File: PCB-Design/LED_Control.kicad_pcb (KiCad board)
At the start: 2 copper layers, 60 x 80 mm, 28 parts, among them J1 5V 5A Power, J2 TO WS2812B LED STRIP, J3 Sound Sensor, SW1 SW_Push_Dual

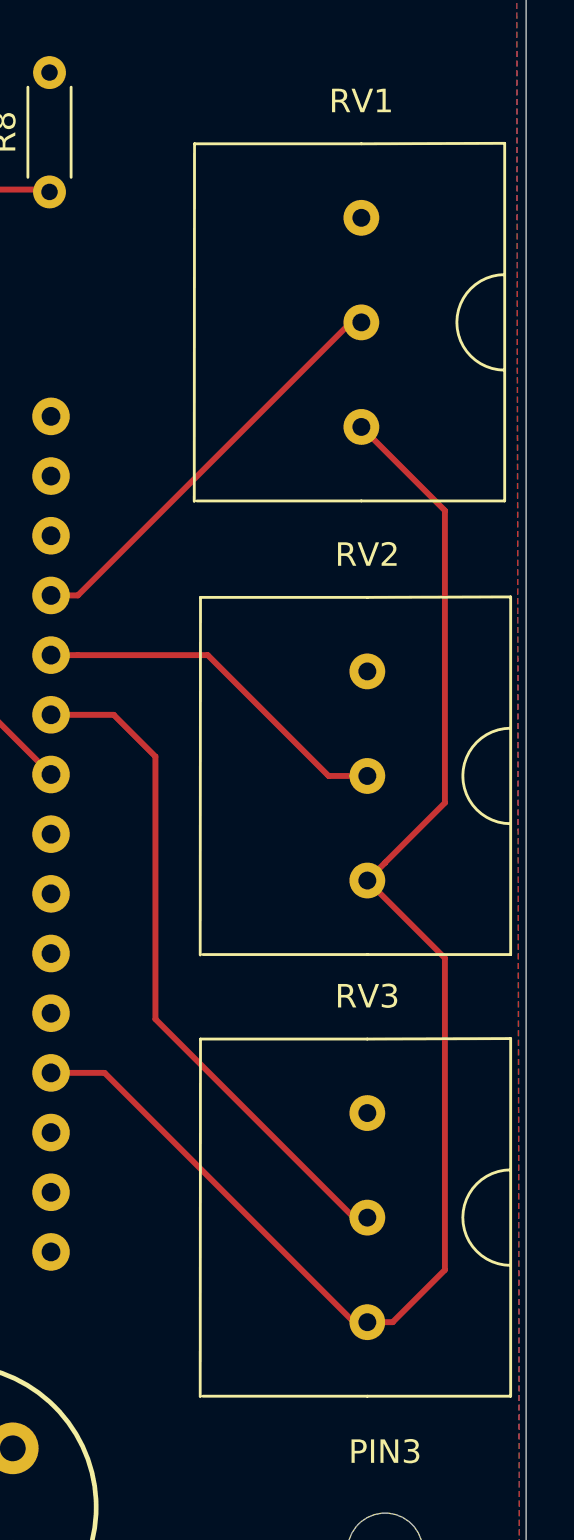
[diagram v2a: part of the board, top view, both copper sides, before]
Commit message: potentiometer footprint fixed
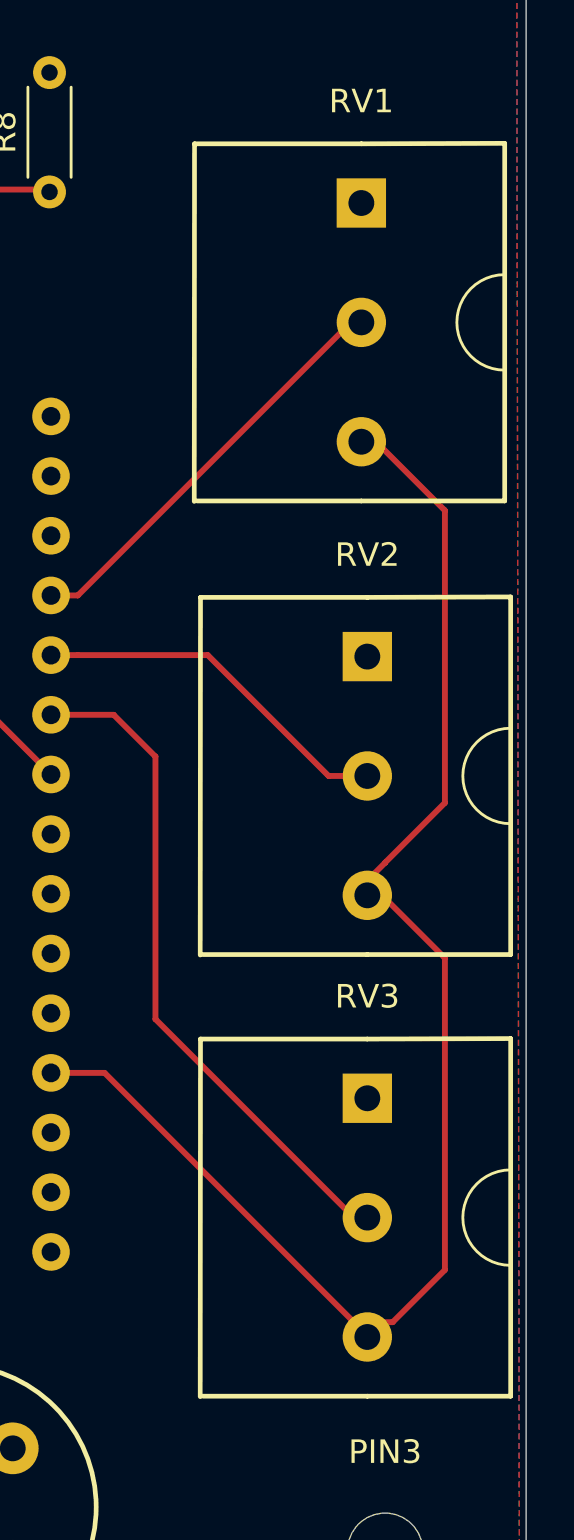
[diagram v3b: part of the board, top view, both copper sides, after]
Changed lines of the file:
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@@
     (add_net VCC)
+  )
+  (module "Custom Footprint:Potentiometer_4mm_Pitch" (layer F.Cu)
+    (at 158.242 119.8245)
+    (fp_text reference RV3 (at 0 -9.406) (layer F.SilkS)
+      (effects (font (size 1 1) (thickness 0.15)))
+    )
+    (fp_text value 100k (at -5.5245 8.8265) (layer F.Fab)
+      (effects (font (size 1 1) (thickness 0.15)))
+    )
+    (fp_line (start 6.096 7.62) (end -7.112 7.62) (layer F.Fab) (width 0.12))
+    (fp_line (start 6.096 -7.62) (end 6.096 7.62) (layer F.Fab) (width 0.12))
+    (fp_line (start -7.112 -7.62) (end 6.096 -7.62) (layer F.Fab) (width 0.12))
+    (fp_line (start -7.112 -7.62) (end -7.112 7.62) (layer F.Fab) (width 0.12))
+    (fp_arc (start 6.096 0) (end 6.096 -2.032) (angle -180) (layer F.SilkS) (width 0.12))
+    (fp_line (start 6.1 -7.62) (end 6.1 7.6) (layer F.SilkS) (width 0.2))
+    (fp_line (start 0 7.6) (end 6.1 7.6) (layer F.SilkS) (width 0.2))
+    (fp_line (start 0 -7.6) (end 6.1 -7.62) (layer F.SilkS) (width 0.2))
+    (fp_line (start -7.1 -7.6) (end -7.112 7.62) (layer F.SilkS) (width 0.2))
+    (fp_line (start 0 7.6) (end -7 7.6) (layer F.SilkS) (width 0.2))
+    (fp_line (start 0 -7.6) (end -7.1 -7.6) (layer F.SilkS) (width 0.2))
+    (pad 3 thru_hole circle (at 0 5.08) (size 2.1 2.1) (drill 1.1) (layers *.Cu *.Mask)
+      (net 21 "Net-(A1-Pad27)"))
+    (pad 2 thru_hole circle (at 0 0) (size 2.1 2.1) (drill 1.1) (layers *.Cu *.Mask)
+      (net 10 "Net-(A1-Pad21)"))
+    (pad 1 thru_hole trapezoid (at 0 -5.08) (size 2.1 2.1) (drill 1.1) (layers *.Cu *.Mask)
+      (net 25 GND))
+  )
+  (module "Custom Footprint:Potentiometer_4mm_Pitch" (layer F.Cu)
+    (at 158.242 101.0285)
+    (fp_text reference RV2 (at 0 -9.406) (layer F.SilkS)
+      (effects (font (size 1 1) (thickness 0.15)))
+    )
+    (fp_text value 100k (at -5.334 8.6995) (layer F.Fab)
+      (effects (font (size 1 1) (thickness 0.15)))
+    )
+    (fp_line (start 6.096 7.62) (end -7.112 7.62) (layer F.Fab) (width 0.12))
+    (fp_line (start 6.096 -7.62) (end 6.096 7.62) (layer F.Fab) (width 0.12))
+    (fp_line (start -7.112 -7.62) (end 6.096 -7.62) (layer F.Fab) (width 0.12))
+    (fp_line (start -7.112 -7.62) (end -7.112 7.62) (layer F.Fab) (width 0.12))
+    (fp_arc (start 6.096 0) (end 6.096 -2.032) (angle -180) (layer F.SilkS) (width 0.12))
+    (fp_line (start 6.1 -7.62) (end 6.1 7.6) (layer F.SilkS) (width 0.2))
+    (fp_line (start 0 7.6) (end 6.1 7.6) (layer F.SilkS) (width 0.2))
+    (fp_line (start 0 -7.6) (end 6.1 -7.62) (layer F.SilkS) (width 0.2))
+    (fp_line (start -7.1 -7.6) (end -7.112 7.62) (layer F.SilkS) (width 0.2))
+    (fp_line (start 0 7.6) (end -7 7.6) (layer F.SilkS) (width 0.2))
+    (fp_line (start 0 -7.6) (end -7.1 -7.6) (layer F.SilkS) (width 0.2))
+    (pad 3 thru_hole circle (at 0 5.08) (size 2.1 2.1) (drill 1.1) (layers *.Cu *.Mask)
+      (net 21 "Net-(A1-Pad27)"))
+    (pad 2 thru_hole circle (at 0 0) (size 2.1 2.1) (drill 1.1) (layers *.Cu *.Mask)
+      (net 8 "Net-(A1-Pad20)"))
+    (pad 1 thru_hole trapezoid (at 0 -5.08) (size 2.1 2.1) (drill 1.1) (layers *.Cu *.Mask)
+      (net 25 GND))
+  )
+  (module "Custom Footprint:Potentiometer_4mm_Pitch" (layer F.Cu)
+    (at 157.988 81.7245)
+    (fp_text reference RV1 (at 0 -9.406) (layer F.SilkS)
+      (effects (font (size 1 1) (thickness 0.15)))
+    )
+    (fp_text value 100k (at -4.953 8.6995) (layer F.Fab)
+      (effects (font (size 1 1) (thickness 0.15)))
+    )
+    (fp_line (start 6.096 7.62) (end -7.112 7.62) (layer F.Fab) (width 0.12))
+    (fp_line (start 6.096 -7.62) (end 6.096 7.62) (layer F.Fab) (width 0.12))
+    (fp_line (start -7.112 -7.62) (end 6.096 -7.62) (layer F.Fab) (width 0.12))
+    (fp_line (start -7.112 -7.62) (end -7.112 7.62) (layer F.Fab) (width 0.12))
+    (fp_arc (start 6.096 0) (end 6.096 -2.032) (angle -180) (layer F.SilkS) (width 0.12))
+    (fp_line (start 6.1 -7.62) (end 6.1 7.6) (layer F.SilkS) (width 0.2))
+    (fp_line (start 0 7.6) (end 6.1 7.6) (layer F.SilkS) (width 0.2))
+    (fp_line (start 0 -7.6) (end 6.1 -7.62) (layer F.SilkS) (width 0.2))
+    (fp_line (start -7.1 -7.6) (end -7.112 7.62) (layer F.SilkS) (width 0.2))
+    (fp_line (start 0 7.6) (end -7 7.6) (layer F.SilkS) (width 0.2))
+    (fp_line (start 0 -7.6) (end -7.1 -7.6) (layer F.SilkS) (width 0.2))
+    (pad 3 thru_hole circle (at 0 5.08) (size 2.1 2.1) (drill 1.1) (layers *.Cu *.Mask)
+      (net 21 "Net-(A1-Pad27)"))
+    (pad 2 thru_hole circle (at 0 0) (size 2.1 2.1) (drill 1.1) (layers *.Cu *.Mask)
+      (net 6 "Net-(A1-Pad19)"))
+    (pad 1 thru_hole trapezoid (at 0 -5.08) (size 2.1 2.1) (drill 1.1) (layers *.Cu *.Mask)
+      (net 25 GND))
   )
   (module Resistor_THT:R_Axial_DIN0204_L3.6mm_D1.6mm_P5.08mm_Horizontal (layer F.Cu)
@@
     )
   )
-  (module "Custom Footprint:Potentiometer_4mm_Pitch" (layer F.Cu)
-    (at 157.988 81.7245)
-    (fp_text reference RV1 (at 0 -9.406) (layer F.SilkS)
-      (effects (font (size 1 1) (thickness 0.15)))
-    )
-    (fp_text value 100k (at -4.953 8.6995) (layer F.Fab)
-      (effects (font (size 1 1) (thickness 0.15)))
-    )
-    (fp_arc (start 6.096 0) (end 6.096 -2.032) (angle -180) (layer F.SilkS) (width 0.12))
-    (fp_line (start 6.1 -7.62) (end 6.1 7.6) (layer F.SilkS) (width 0.12))
-    (fp_line (start 0 7.6) (end 6.1 7.6) (layer F.SilkS) (width 0.12))
-    (fp_line (start 0 -7.6) (end 6.1 -7.62) (layer F.SilkS) (width 0.12))
-    (fp_line (start -7.1 -7.6) (end -7.112 7.62) (layer F.SilkS) (width 0.12))
-    (fp_line (start 0 7.6) (end -7 7.6) (layer F.SilkS) (width 0.12))
-    (fp_line (start 0 -7.6) (end -7.1 -7.6) (layer F.SilkS) (width 0.12))
-    (pad 3 thru_hole circle (at 0 4.45) (size 1.524 1.524) (drill 0.762) (layers *.Cu *.Mask)
-      (net 21 "Net-(A1-Pad27)"))
-    (pad 2 thru_hole circle (at 0 0) (size 1.524 1.524) (drill 0.762) (layers *.Cu *.Mask)
-      (net 6 "Net-(A1-Pad19)"))
-    (pad 1 thru_hole circle (at 0 -4.45) (size 1.524 1.524) (drill 0.762) (layers *.Cu *.Mask)
-      (net 25 GND))
-  )
-  (module "Custom Footprint:Potentiometer_4mm_Pitch" (layer F.Cu)
-    (at 158.242 101.0285)
-    (fp_text reference RV2 (at 0 -9.406) (layer F.SilkS)
-      (effects (font (size 1 1) (thickness 0.15)))
-    )
-    (fp_text value 100k (at -5.334 8.6995) (layer F.Fab)
-      (effects (font (size 1 1) (thickness 0.15)))
-    )
-    (fp_line (start 0 -7.6) (end -7.1 -7.6) (layer F.SilkS) (width 0.12))
-    (fp_line (start 0 7.6) (end -7 7.6) (layer F.SilkS) (width 0.12))
-    (fp_line (start -7.1 -7.6) (end -7.112 7.62) (layer F.SilkS) (width 0.12))
-    (fp_line (start 0 -7.6) (end 6.1 -7.62) (layer F.SilkS) (width 0.12))
-    (fp_line (start 0 7.6) (end 6.1 7.6) (layer F.SilkS) (width 0.12))
-    (fp_line (start 6.1 -7.62) (end 6.1 7.6) (layer F.SilkS) (width 0.12))
-    (fp_arc (start 6.096 0) (end 6.096 -2.032) (angle -180) (layer F.SilkS) (width 0.12))
-    (pad 1 thru_hole circle (at 0 -4.45) (size 1.524 1.524) (drill 0.762) (layers *.Cu *.Mask)
-      (net 25 GND))
-    (pad 2 thru_hole circle (at 0 0) (size 1.524 1.524) (drill 0.762) (layers *.Cu *.Mask)
-      (net 8 "Net-(A1-Pad20)"))
-    (pad 3 thru_hole circle (at 0 4.45) (size 1.524 1.524) (drill 0.762) (layers *.Cu *.Mask)
-      (net 21 "Net-(A1-Pad27)"))
-  )
-  (module "Custom Footprint:Potentiometer_4mm_Pitch" (layer F.Cu)
-    (at 158.242 119.8245)
-    (fp_text reference RV3 (at 0 -9.406) (layer F.SilkS)
-      (effects (font (size 1 1) (thickness 0.15)))
-    )
-    (fp_text value 100k (at -5.5245 8.8265) (layer F.Fab)
-      (effects (font (size 1 1) (thickness 0.15)))
-    )
-    (fp_line (start 0 -7.6) (end -7.1 -7.6) (layer F.SilkS) (width 0.12))
-    (fp_line (start 0 7.6) (end -7 7.6) (layer F.SilkS) (width 0.12))
-    (fp_line (start -7.1 -7.6) (end -7.112 7.62) (layer F.SilkS) (width 0.12))
-    (fp_line (start 0 -7.6) (end 6.1 -7.62) (layer F.SilkS) (width 0.12))
-    (fp_line (start 0 7.6) (end 6.1 7.6) (layer F.SilkS) (width 0.12))
-    (fp_line (start 6.1 -7.62) (end 6.1 7.6) (layer F.SilkS) (width 0.12))
-    (fp_arc (start 6.096 0) (end 6.096 -2.032) (angle -180) (layer F.SilkS) (width 0.12))
-    (pad 1 thru_hole circle (at 0 -4.45) (size 1.524 1.524) (drill 0.762) (layers *.Cu *.Mask)
-      (net 25 GND))
-    (pad 2 thru_hole circle (at 0 0) (size 1.524 1.524) (drill 0.762) (layers *.Cu *.Mask)
-      (net 10 "Net-(A1-Pad21)"))
-    (pad 3 thru_hole circle (at 0 4.45) (size 1.524 1.524) (drill 0.762) (layers *.Cu *.Mask)
-      (net 21 "Net-(A1-Pad27)"))
-  )
   (module "Custom Footprint:Push_Button_Switch" (layer F.Cu)

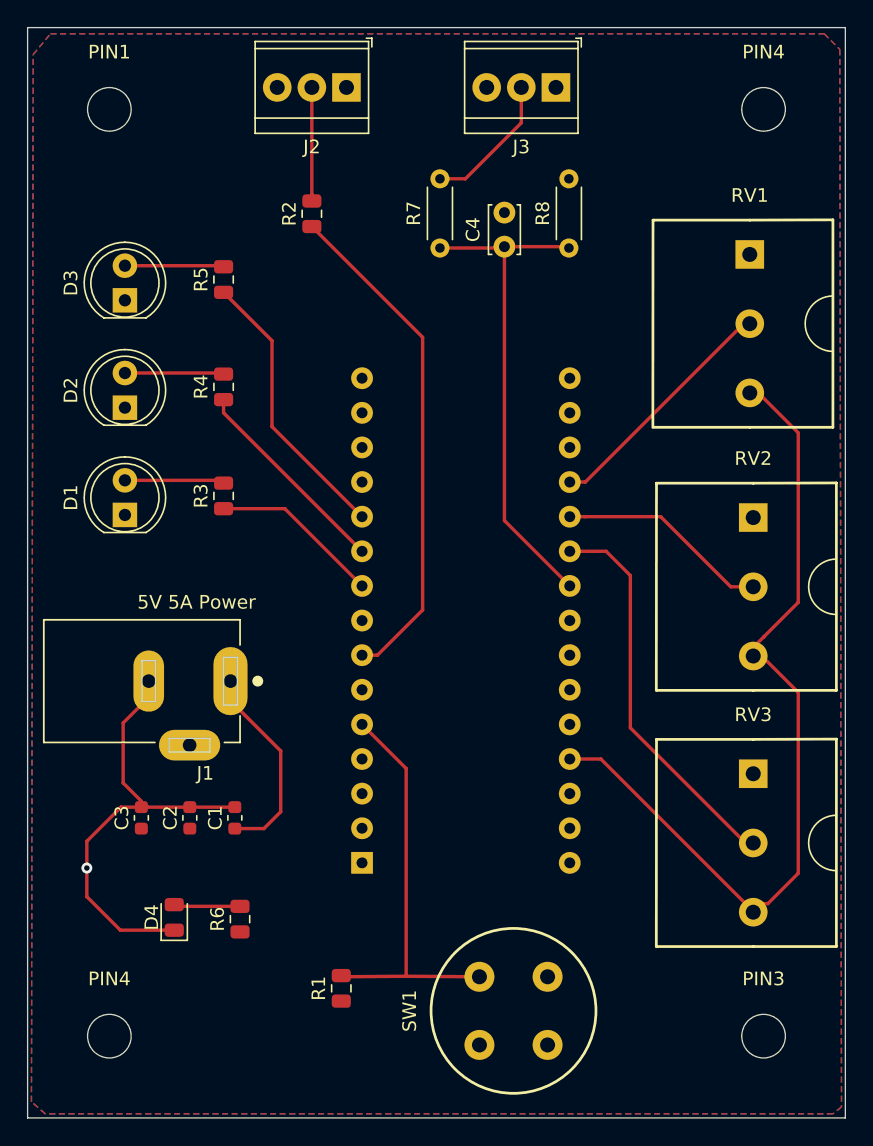
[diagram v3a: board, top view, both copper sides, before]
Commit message: Rev 2. alterations to PCB
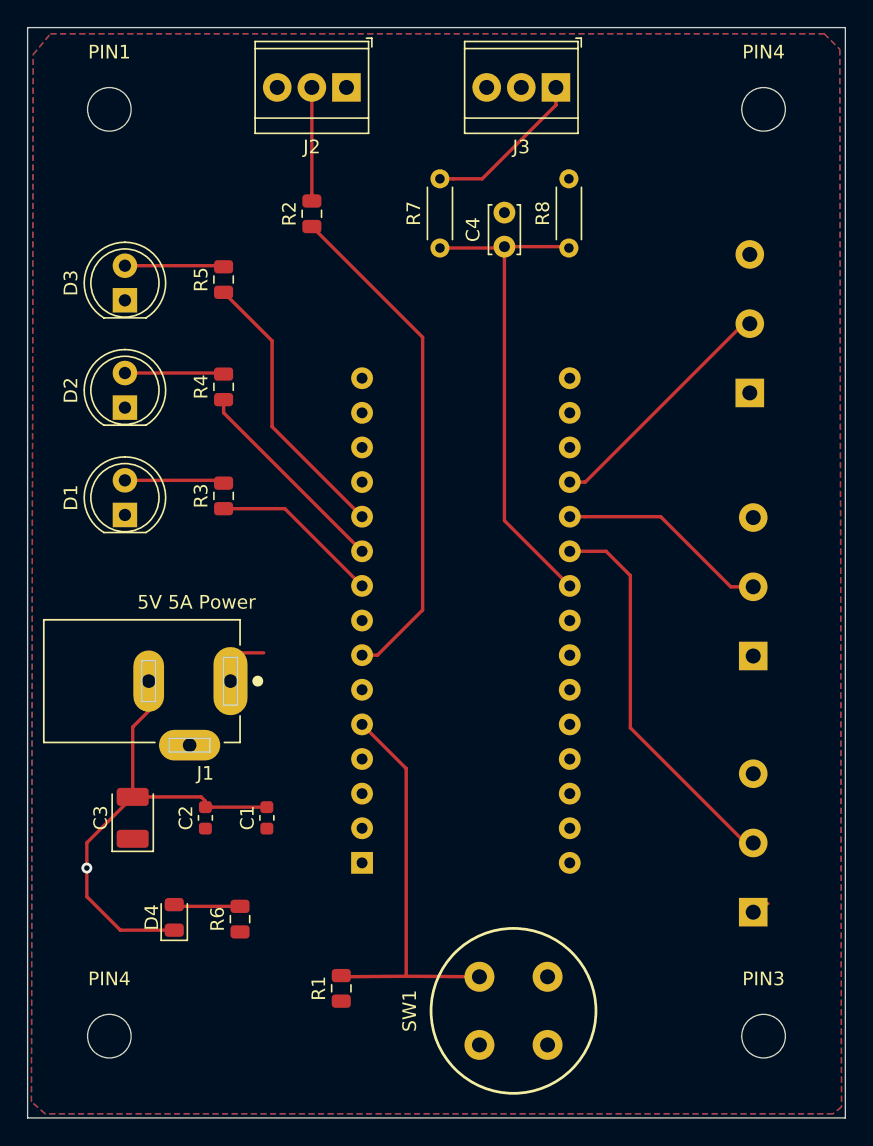
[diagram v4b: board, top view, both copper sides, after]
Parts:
- C3: value 0.1uF -> 100uF; footprint Capacitor_SMD:C_0603_1608Metric -> Capacitor_Tantalum_SMD:CP_EIA-3528-15_AVX-H
- R6: value 200 -> 300
- RV1, RV2, RV3: footprint Custom Footprint:Potentiometer_4mm_Pitch -> Custom Footprint:Potentiometer_5.08mm_Pitch; moved to B.Cu
- moved C1 2.35 mm to (122.6, 118.0)
- moved C2 1.14 mm to (118.0, 118.0)
- moved C3 0.63 mm to (112.7, 118.0)
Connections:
- J3 pad 1: VCC -> /SS_DATA_OUT
- J3 pad 2: /SS_DATA_OUT -> GND
- J3 pad 3: GND -> VCC
- RV1 pad 3: Net-(A1-Pad27) -> VCC
- RV2 pad 3: Net-(A1-Pad27) -> VCC
- RV3 pad 3: Net-(A1-Pad27) -> VCC
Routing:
- net Net-(A1-Pad27): track 61.7 -> 0.00 mm
- net VCC: track 14.0 -> 6.97 mm
- net GND: track 31.9 -> 34.9 mm
- net /SS_DATA_OUT: track 10.3 -> 12.0 mm
